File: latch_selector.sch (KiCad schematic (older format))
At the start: 33 parts, among them SW1 SW_DIP_x03, SW3 SW_Push, SW4 Run/Step Mode, U11 74HCT00, U12 74HCT74, U13 MAX6816, U14 LMC555xN, U4 74HCT138, U5 74HCT151, U6 74HCT32

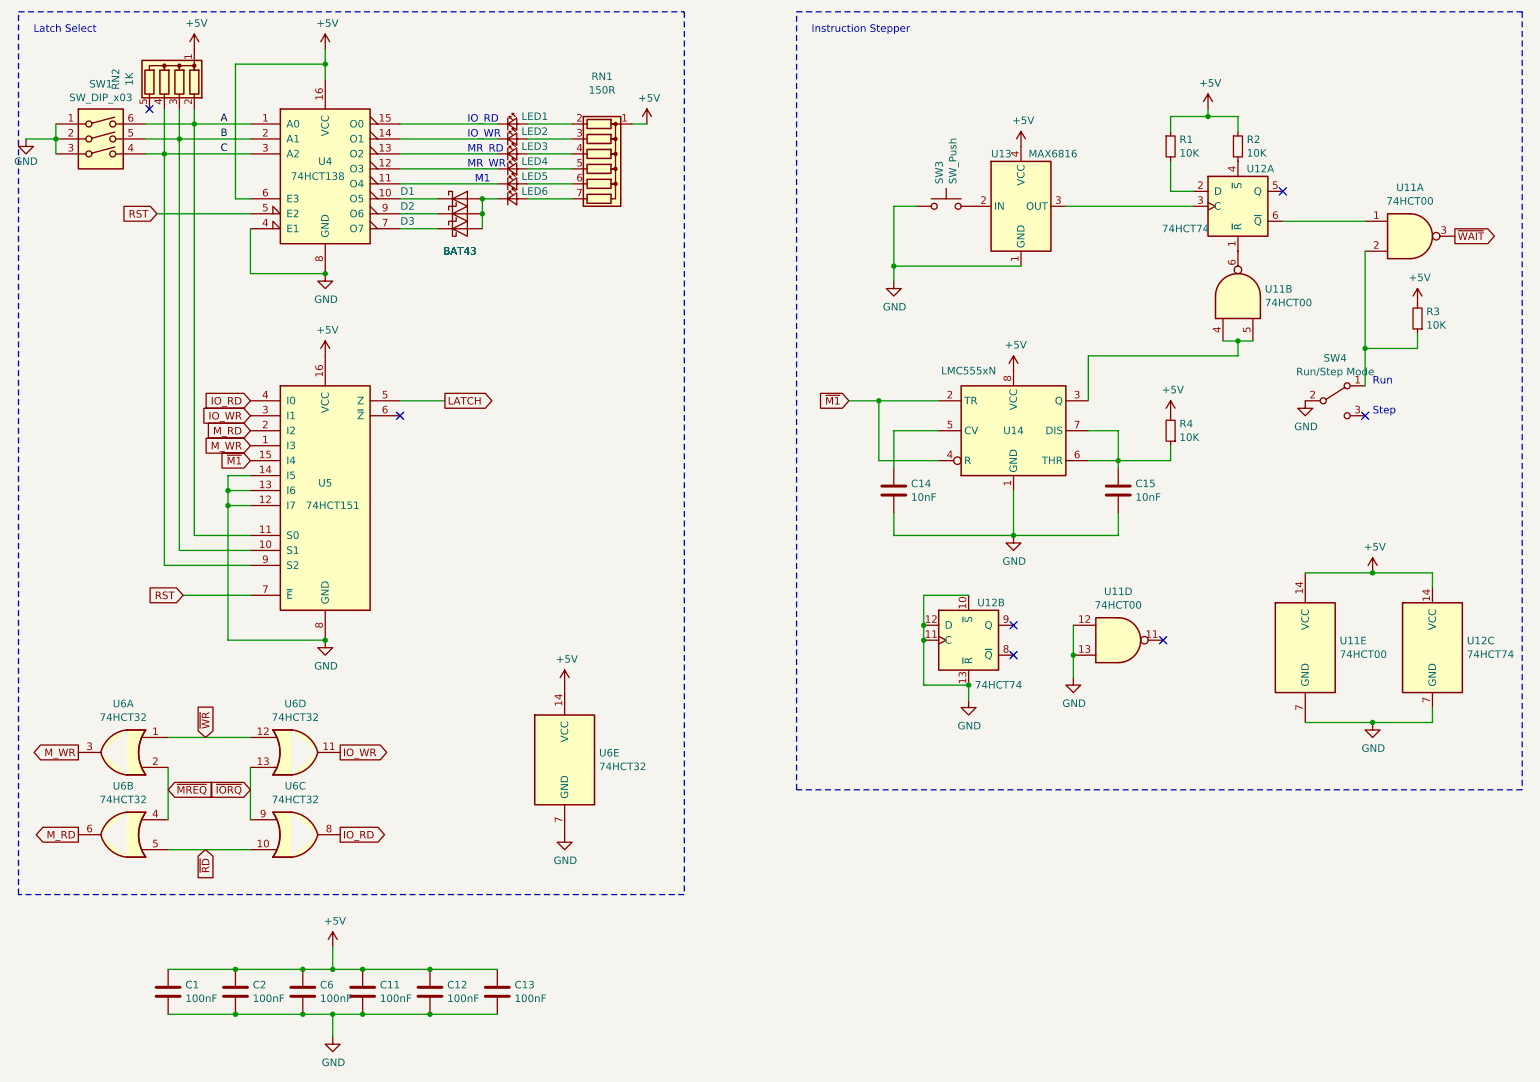
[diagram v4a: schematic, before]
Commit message: SMD version
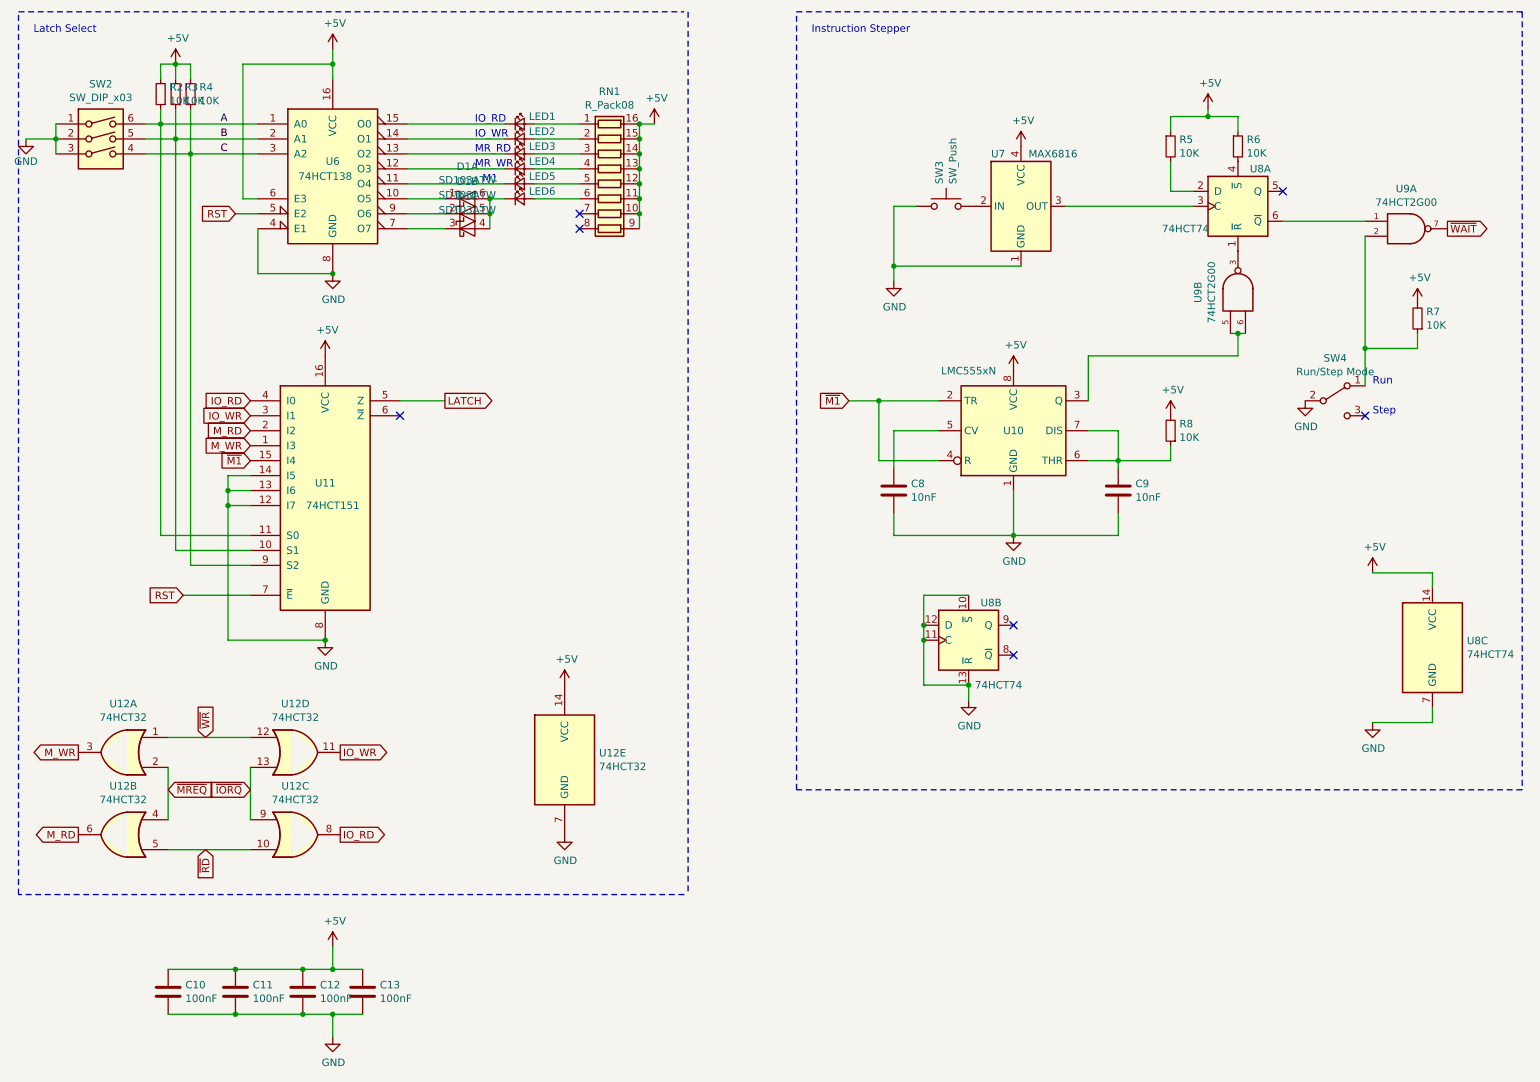
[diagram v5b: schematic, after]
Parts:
- removed C12, C13: 100nF, Capacitor_SMD:C_0805_2012Metric_Pad1.15x1.40mm_HandSolder, symbol Device:C
- removed D1, D2, D3: BAT43, Diode_THT:D_DO-35_SOD27_P7.62mm_Horizontal, symbol Diode:BAT43
- removed RN1: 150R, Resistor_THT:R_Array_SIP7, symbol Device:R_Network06
- removed RN2: 1K, Resistor_THT:R_Array_SIP5, symbol Device:R_Network04
- removed U11: 74HCT00, Package_DIP:DIP-14_W7.62mm, symbol 74xx:74HCT00
- added D1: SD103ATW, Package_TO_SOT_SMD:SOT-363_SC-70-6, symbol Diode:SD103ATW
- added R2, R3, R4: 10K, Resistor_SMD:R_0603_1608Metric_Pad1.05x0.95mm_HandSolder, symbol Device:R_Small
- added RN1: R_Pack08, Resistor_SMD:R_Cat16-8, symbol Device:R_Pack08
- added U9: 74HCT2G00, Package_SO:TSSOP-8_3x3mm_P0.65mm, symbol 74xGxx:74LVC2G00
- C10: renamed from C1; footprint Capacitor_SMD:C_0805_2012Metric_Pad1.15x1.40mm_HandSolder -> Capacitor_SMD:C_0603_1608Metric_Pad1.05x0.95mm_HandSolder
- C11: renamed from C2; footprint Capacitor_SMD:C_0805_2012Metric_Pad1.15x1.40mm_HandSolder -> Capacitor_SMD:C_0603_1608Metric_Pad1.05x0.95mm_HandSolder
- C12: renamed from C6; footprint Capacitor_SMD:C_0805_2012Metric_Pad1.15x1.40mm_HandSolder -> Capacitor_SMD:C_0603_1608Metric_Pad1.05x0.95mm_HandSolder
- C13: renamed from C11; footprint Capacitor_SMD:C_0805_2012Metric_Pad1.15x1.40mm_HandSolder -> Capacitor_SMD:C_0603_1608Metric_Pad1.05x0.95mm_HandSolder
- C8: renamed from C14; footprint Capacitor_SMD:C_0805_2012Metric_Pad1.15x1.40mm_HandSolder -> Capacitor_SMD:C_0603_1608Metric_Pad1.05x0.95mm_HandSolder
- C9: renamed from C15; footprint Capacitor_SMD:C_0805_2012Metric_Pad1.15x1.40mm_HandSolder -> Capacitor_SMD:C_0603_1608Metric_Pad1.05x0.95mm_HandSolder
- LED1, LED2, LED3, LED4, LED5, LED6: footprint LED_SMD:LED_0805_2012Metric_Pad1.15x1.40mm_HandSolder -> LED_SMD:LED_0603_1608Metric_Pad1.05x0.95mm_HandSolder
- R5: renamed from R1; footprint Resistor_SMD:R_0805_2012Metric_Pad1.15x1.40mm_HandSolder -> Resistor_SMD:R_0603_1608Metric_Pad1.05x0.95mm_HandSolder
- R6: renamed from R2; footprint Resistor_SMD:R_0805_2012Metric_Pad1.15x1.40mm_HandSolder -> Resistor_SMD:R_0603_1608Metric_Pad1.05x0.95mm_HandSolder
- R7: renamed from R3; footprint Resistor_SMD:R_0805_2012Metric_Pad1.15x1.40mm_HandSolder -> Resistor_SMD:R_0603_1608Metric_Pad1.05x0.95mm_HandSolder
- R8: renamed from R4; footprint Resistor_SMD:R_0805_2012Metric_Pad1.15x1.40mm_HandSolder -> Resistor_SMD:R_0603_1608Metric_Pad1.05x0.95mm_HandSolder
- U10: renamed from U14; footprint Package_DIP:DIP-8_W7.62mm -> Package_SO:SOIC-8_3.9x4.9mm_P1.27mm
- U11: renamed from U5; footprint Package_DIP:DIP-16_W7.62mm -> Package_SO:TSSOP-16_4.4x5mm_P0.65mm
- U12: renamed from U6; footprint Package_DIP:DIP-14_W7.62mm -> Package_SO:TSSOP-14_4.4x5mm_P0.65mm
- U6: renamed from U4; footprint Package_DIP:DIP-16_W7.62mm -> Package_SO:TSSOP-16_4.4x5mm_P0.65mm
- U8: renamed from U12; footprint Package_DIP:DIP-14_W7.62mm -> Package_SO:TSSOP-14_4.4x5mm_P0.65mm
- renumbered SW1 to SW2, U13 to U7
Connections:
- net +5V: now also R2.2, R3.2, R4.2, RN1.10 (R7.2), RN1.11 (R6.2), RN1.12 (R5.2), RN1.13 (R4.2), RN1.14 (R3.2), RN1.15 (R2.2), RN1.16 (R1.2), RN1.9 (R8.2)
- net A: now also R2.1
- net B: now also R3.1
- net C: now also R4.1
- net GND: now also U9.4 (GND), U9.4 (GND)
- net ~WAIT: now also U9.7
- net at U8.6 (~Q): now also U9.1
- net at R7.1, SW4.1 (A): now also U9.2
- net at U8.1 (~R): now also U9.3
- net at LED1.2 (A): now also RN1.1 (R1.1)
- net at LED2.2 (A): now also RN1.2 (R2.1)
- net at LED3.2 (A): now also RN1.3 (R3.1)
- net at LED4.2 (A): now also RN1.4 (R4.1)
- net at LED5.2 (A): now also RN1.5 (R5.1)
- net at U6.10 (O5): now also D1.1 (K)
- net at U6.7 (O7): now also D1.3 (K)
- net at U6.9 (O6): now also D1.2 (K)
- net at LED6.2 (A): now also RN1.6 (R6.1)
- net at LED6.1 (K): now also D1.4 (A), D1.5 (A), D1.6 (A)
- net at U10.3 (Q): now also U9.5, U9.6
- new net VCC: U9.8 (VCC), U9.8 (VCC)
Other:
- moved on the sheet: LED1, LED2, LED3, LED4, LED5, LED6, U6
